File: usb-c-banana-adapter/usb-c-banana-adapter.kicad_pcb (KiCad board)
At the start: 2 copper layers, 18 x 31 mm, 5 parts, among them J1 TYPE-C-31-M-12, J2 Conn_01x01, J3 Conn_01x01

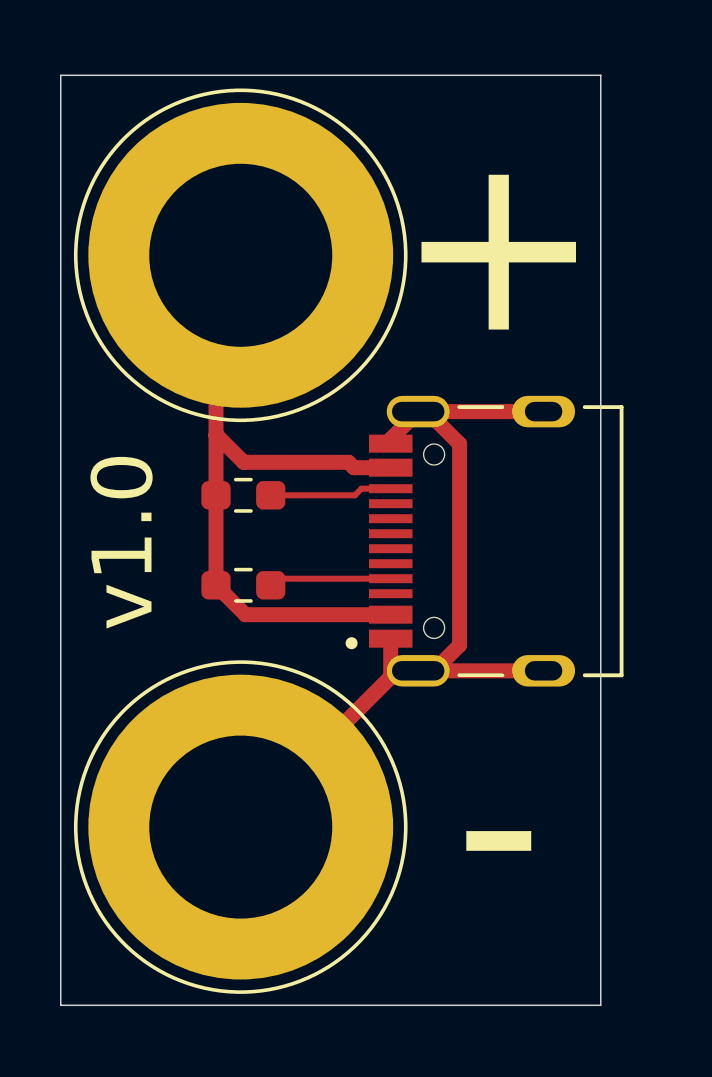
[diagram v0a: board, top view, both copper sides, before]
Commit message: Update for usb-c-banana-adapter v1.0
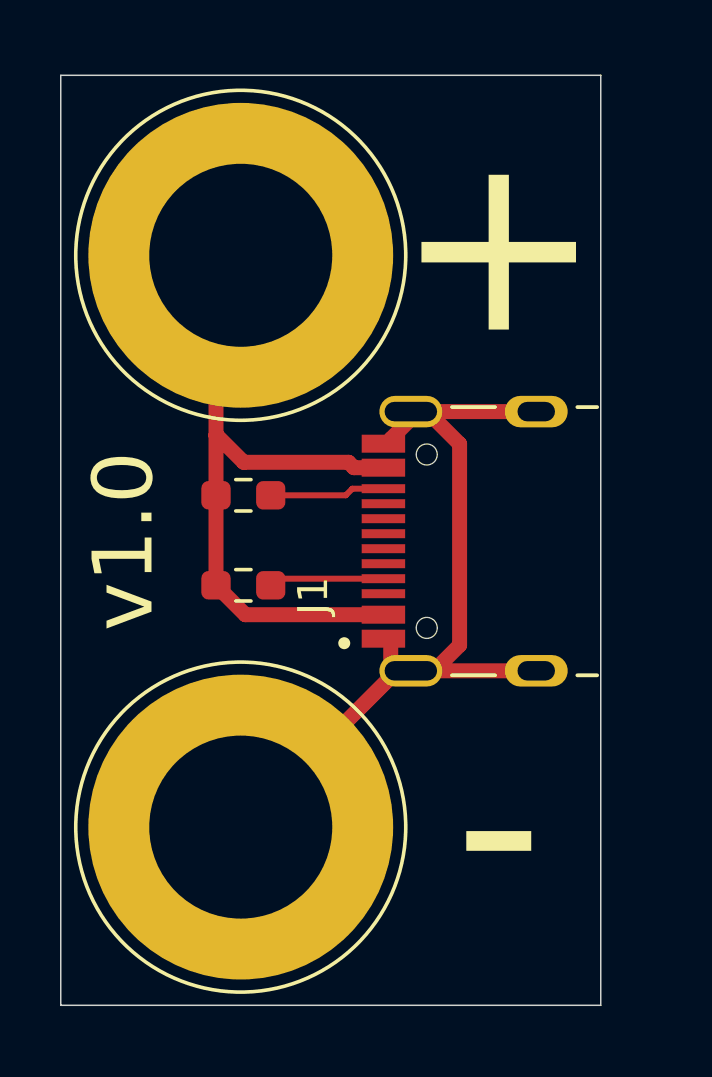
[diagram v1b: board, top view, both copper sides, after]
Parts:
- moved J1 2.72 mm to (107.4, 109.5)
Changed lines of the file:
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@@
 	(footprint "Homebrew:HRO_TYPE-C-31-M-12"
 		(layer "F.Cu")
-		(at 110.095 109.53 90)
+		(at 107.38 109.53 90)
 		(property "Reference" "J1"
-			(at -1.825 -7.435 270)
+			(at -1.825 -4.965 90)
 			(layer "F.SilkS")
-			(hide yes)
 			(effects
 				(font
@@
 		)
 		(property "Value" "TYPE-C-31-M-12"
-			(at 6.43 4.135 270)
+			(at 6.43 6.605 90)
 			(layer "F.Fab")
 			(effects
@@
 		)
 		(property "Footprint" "Homebrew:HRO_TYPE-C-31-M-12"
+			(at 0 2.47 90)
+			(unlocked yes)
+			(layer "F.Fab")
+			(hide yes)
+			(effects
+				(font
+					(size 1.27 1.27)
+				)
+			)
+		)
+		(property "Datasheet" ""
+			(at 0 2.47 90)
+			(unlocked yes)
+			(layer "F.Fab")
+			(hide yes)
+			(effects
+				(font
+					(size 1.27 1.27)
+				)
+			)
+		)
+		(property "Description" ""
+			(at 0 2.47 90)
+			(unlocked yes)
+			(layer "F.Fab")
+			(hide yes)
+			(effects
+				(font
+					(size 1.27 1.27)
+				)
+			)
+		)
+		(property "JLCPCB Position Offset" "0, 3.88"
 			(at 0 0 90)
 			(unlocked yes)
-			(layer "F.Fab")
-			(hide yes)
-			(effects
-				(font
-					(size 1.27 1.27)
-				)
-			)
-		)
-		(property "Datasheet" ""
-			(at 0 0 90)
-			(unlocked yes)
-			(layer "F.Fab")
-			(hide yes)
-			(effects
-				(font
-					(size 1.27 1.27)
-				)
-			)
-		)
-		(property "Description" ""
-			(at 0 0 90)
-			(unlocked yes)
-			(layer "F.Fab")
-			(hide yes)
-			(effects
-				(font
-					(size 1.27 1.27)
+			(layer "F.SilkS")
+			(hide yes)
+			(effects
+				(font
+					(size 1 1)
+					(thickness 0.15)
 				)
 			)
@@
 		(attr through_hole)
 		(fp_line
-			(start 4.47 -2.81)
-			(end 4.47 -1.37)
+			(start 4.47 -0.34)
+			(end 4.47 1.1)
 			(stroke
 				(width 0.127)
@@
 		)
 		(fp_line
-			(start -4.47 -2.81)
-			(end -4.47 -1.37)
+			(start -4.47 -0.34)
+			(end -4.47 1.1)
 			(stroke
 				(width 0.127)
@@
 		)
 		(fp_line
-			(start 4.47 1.37)
-			(end 4.47 2.6)
+			(start 4.47 3.84)
+			(end 4.47 4.5)
 			(stroke
 				(width 0.127)
@@
 		)
 		(fp_line
-			(start 4.47 2.6)
-			(end -4.47 2.6)
+			(start -4.47 4.5)
+			(end -4.47 3.84)
 			(stroke
 				(width 0.127)
@@
 			(layer "F.SilkS")
 		)
-		(fp_line
-			(start -4.47 2.6)
-			(end -4.47 1.37)
-			(stroke
-				(width 0.127)
-				(type solid)
-			)
-			(layer "F.SilkS")
-		)
 		(fp_circle
-			(center -3.4 -6.4)
-			(end -3.3 -6.4)
+			(center -3.4 -3.93)
+			(end -3.3 -3.93)
 			(stroke
 				(width 0.2)
@@
 		)
 		(fp_line
-			(start 0 3.1)
-			(end 0.7 3.8)
+			(start 0 5.57)
+			(end 0.7 6.27)
 			(stroke
 				(width 0.12)
@@
 		)
 		(fp_line
-			(start 0 3.1)
-			(end -0.7 3.8)
+			(start 0 5.57)
+			(end -0.7 6.27)
 			(stroke
 				(width 0.12)
@@
 		)
 		(fp_line
-			(start 0 6.8)
-			(end 0 3.1)
+			(start 0 9.27)
+			(end 0 5.57)
 			(stroke
 				(width 0.12)
@@
 		)
 		(fp_rect
-			(start -5.1 -6.1)
-			(end 5.1 9.4)
+			(start -5.1 -3.63)
+			(end 5.1 11.87)
 			(stroke
 				(width 0.1)
@@
 		)
 		(fp_line
-			(start 4.47 -4.7)
-			(end -4.47 -4.7)
+			(start 4.47 -2.23)
+			(end -4.47 -2.23)
 			(stroke
 				(width 0.127)
@@
 		)
 		(fp_line
-			(start -4.47 -4.7)
-			(end -4.47 2.6)
+			(start -4.47 -2.23)
+			(end -4.47 5.07)
 			(stroke
 				(width 0.127)
@@
 		)
 		(fp_line
-			(start -5.5 2.14)
-			(end 5.6 2.14)
+			(start -5.5 4.61)
+			(end 5.6 4.61)
 			(stroke
 				(width 0.1)
@@
 		)
 		(fp_line
-			(start 4.47 2.6)
-			(end 4.47 -4.7)
+			(start 4.47 5.07)
+			(end 4.47 -2.23)
 			(stroke
 				(width 0.127)
@@
 		)
 		(fp_line
-			(start -4.47 2.6)
-			(end 4.47 2.6)
+			(start -4.47 5.07)
+			(end 4.47 5.07)
 			(stroke
 				(width 0.127)
@@
 		)
 		(fp_rect
-			(start -5.1 -6.1)
-			(end 5.1 2.9)
+			(start -5.1 -3.63)
+			(end 5.1 5.37)
 			(stroke
 				(width 0.1)
@@
 		)
 		(fp_circle
-			(center -3.4 -6.4)
-			(end -3.3 -6.4)
+			(center -3.4 -3.93)
+			(end -3.3 -3.93)
 			(stroke
 				(width 0.2)
@@
 		)
 		(pad "" np_thru_hole circle
-			(at -2.89 -3.65 90)
+			(at -2.89 -1.18 90)
 			(size 0.7 0.7)
 			(drill 0.7)
@@
 		)
 		(pad "" np_thru_hole circle
-			(at 2.89 -3.65 90)
+			(at 2.89 -1.18 90)
 			(size 0.7 0.7)
 			(drill 0.7)
@@
 		)
 		(pad "A1B12" smd rect
-			(at -3.25 -5.095 90)
+			(at -3.25 -2.625 90)
 			(size 0.6 1.45)
 			(layers "F.Cu" "F.Paste" "F.Mask")
@@
 		)
 		(pad "A4B9" smd rect
-			(at -2.45 -5.095 90)
+			(at -2.45 -2.625 90)
 			(size 0.6 1.45)
 			(layers "F.Cu" "F.Paste" "F.Mask")
@@
 		)
 		(pad "A5" smd rect
-			(at -1.25 -5.095 90)
+			(at -1.25 -2.625 90)
 			(size 0.3 1.45)
 			(layers "F.Cu" "F.Paste" "F.Mask")
@@
 		)
 		(pad "A6" smd rect
-			(at -0.25 -5.095 90)
+			(at -0.25 -2.625 90)
 			(size 0.3 1.45)
 			(layers "F.Cu" "F.Paste" "F.Mask")
@@
 		)
 		(pad "A7" smd rect
-			(at 0.25 -5.095 90)
+			(at 0.25 -2.625 90)
 			(size 0.3 1.45)
 			(layers "F.Cu" "F.Paste" "F.Mask")
@@
 		)
 		(pad "A8" smd rect
-			(at 1.25 -5.095 90)
+			(at 1.25 -2.625 90)
 			(size 0.3 1.45)
 			(layers "F.Cu" "F.Paste" "F.Mask")
@@
 		)
 		(pad "B1A12" smd rect
-			(at 3.25 -5.095 90)
+			(at 3.25 -2.625 90)
 			(size 0.6 1.45)
 			(layers "F.Cu" "F.Paste" "F.Mask")
@@
 		)
 		(pad "B4A9" smd rect
-			(at 2.45 -5.095 90)
+			(at 2.45 -2.625 90)
 			(size 0.6 1.45)
 			(layers "F.Cu" "F.Paste" "F.Mask")
@@
 		)
 		(pad "B5" smd rect
-			(at 1.75 -5.095 90)
+			(at 1.75 -2.625 90)
 			(size 0.3 1.45)
 			(layers "F.Cu" "F.Paste" "F.Mask")
@@
 		)
 		(pad "B6" smd rect
-			(at 0.75 -5.095 90)
+			(at 0.75 -2.625 90)
 			(size 0.3 1.45)
 			(layers "F.Cu" "F.Paste" "F.Mask")
@@
 		)
 		(pad "B7" smd rect
-			(at -0.75 -5.095 90)
+			(at -0.75 -2.625 90)
 			(size 0.3 1.45)
 			(layers "F.Cu" "F.Paste" "F.Mask")
@@
 		)
 		(pad "B8" smd rect
-			(at -1.75 -5.095 90)
+			(at -1.75 -2.625 90)
 			(size 0.3 1.45)
 			(layers "F.Cu" "F.Paste" "F.Mask")
@@
 		)
 		(pad "S1" thru_hole oval
-			(at -4.32 -4.18 90)
+			(at -4.32 -1.71 90)
 			(size 1.05 2.1)
 			(drill oval 0.65 1.75)
@@
 		)
 		(pad "S2" thru_hole oval
-			(at 4.32 -4.18 90)
+			(at 4.32 -1.71 90)
 			(size 1.05 2.1)
 			(drill oval 0.65 1.75)
@@
 		)
 		(pad "S3" thru_hole oval
-			(at -4.32 0 90)
+			(at -4.32 2.47 90)
 			(size 1.05 2.1)
 			(drill oval 0.65 1.25)
@@
 		)
 		(pad "S4" thru_hole oval
-			(at 4.32 0 90)
+			(at 4.32 2.47 90)
 			(size 1.05 2.1)
 			(drill oval 0.65 1.25)
@@
 		(model "${HOMEBREW}/TYPE-C-31-M-12.wrl"
 			(offset
-				(xyz 0 0 0)
+				(xyz 0 -2.47 0)
 			)
 			(scale
@@
 	(segment
 		(start 105 107.78)
-		(end 104.025 107.78)
+		(end 103.72 107.78)
 		(width 0.2)
 		(layer "F.Cu")
@@
 	)
 	(segment
-		(start 103.805 108)
+		(start 103.72 107.78)
+		(end 103.5 108)
+		(width 0.2)
+		(layer "F.Cu")
+		(net 3)
+	)
+	(segment
+		(start 103.5 108)
 		(end 101 108)
 		(width 0.2)
 		(layer "F.Cu")
-		(net 3)
-	)
-	(segment
-		(start 104.025 107.78)
-		(end 103.805 108)
-		(width 0.2)
-		(layer "F.Cu")
